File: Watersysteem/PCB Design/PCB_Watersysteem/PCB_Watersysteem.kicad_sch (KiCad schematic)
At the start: 54 parts, among them J1 Screw_Terminal_01x02, J10 LED Water Level, J11 LED Nutrient Level, J12 Height Nutrients, J13 Height Mixer, J2 Conn_01x04_Pin, J21 Voedingstoffen 1, J3 ReferentieProbe, J4 Voedingstoffen 2, J5 Voedingstoffen 3, J6 Height Water, J7 Endstop Lade0, J8 Endstop Lade1, J9 Endstop UV, SW1 EN, SW2 BOOT, U1 ESP32-WROOM-32D, U2 MP1584_Module, U3 AMS1117-3.3, U4 ADS1115IDGS, U5 MCP23017_SO

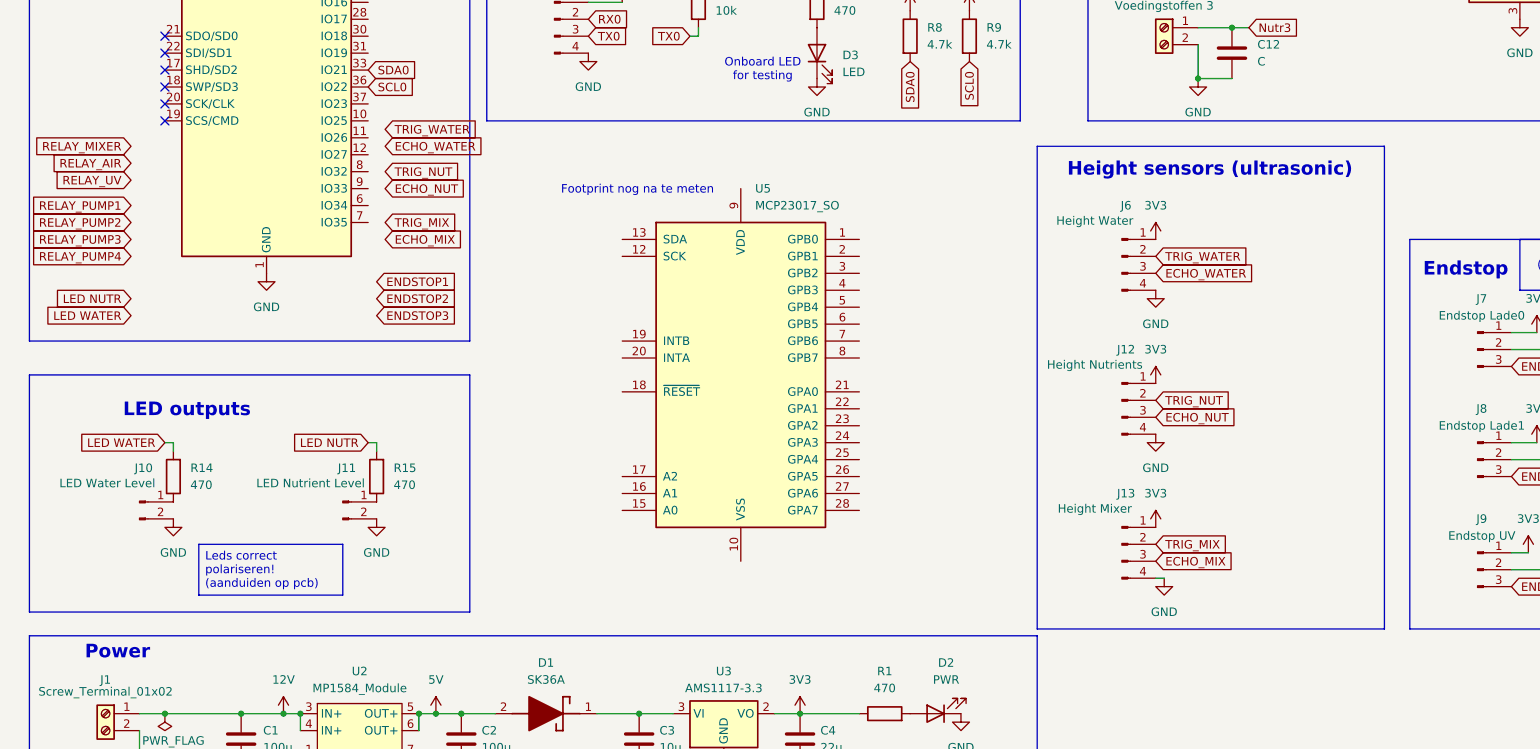
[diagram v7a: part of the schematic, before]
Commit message: Update PCB
16 bit IO-expander ingesteld
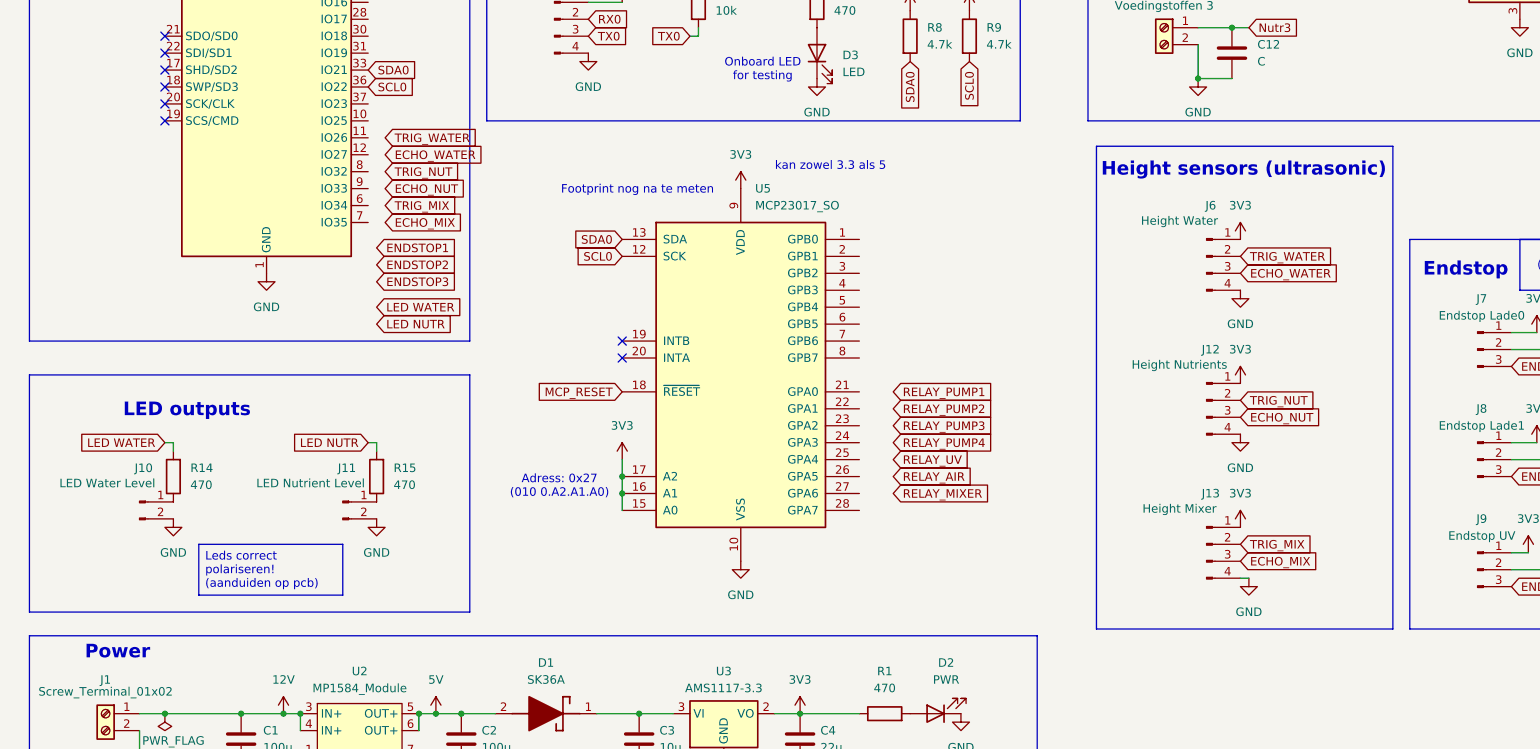
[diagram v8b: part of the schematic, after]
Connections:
- net 3V3: now also U5.15 (A0), U5.16 (A1), U5.17 (A2), U5.9 (VDD)
- net GND: now also U5.10 (VSS)
- net SCL0: now also U5.12 (SCK)
- net SDA0: now also U5.13 (SDA)
- net MCP_RESET: now reaches U5.18 (~{RESET})
- no-connect marks 9 -> 11
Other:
- note added: "Adress: 0x27 (010 0.A2.A1.A0)"
- note added: "kan zowel 3.3 als 5"
- moved on the sheet: J12, J13, J6
